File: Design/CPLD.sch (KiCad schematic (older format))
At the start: 1 part, among them U5 5M40ZE64C5N

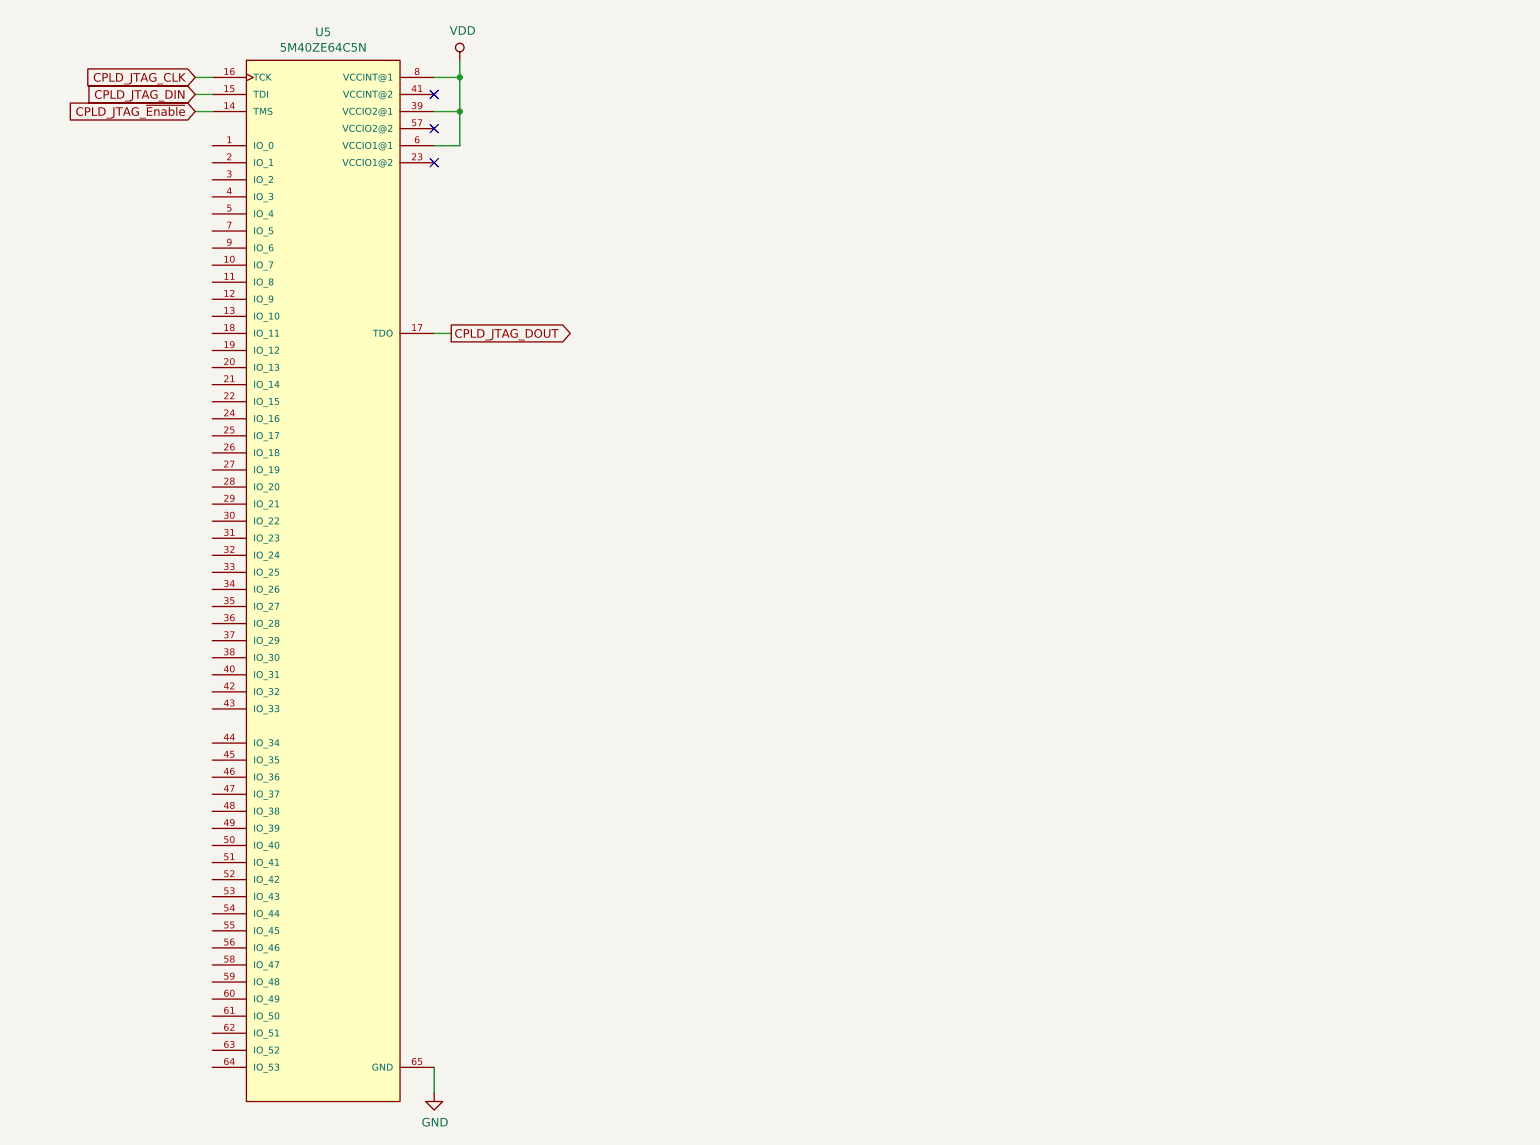
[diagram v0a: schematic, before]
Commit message: Improvement over the Power management: - added TPS6201DRC for raising leaking voltage from supercapacitor - supercap is protected from overvoltage using a shunt diode - power management is using MOSFET logic (2 PFET, 1 NFET)
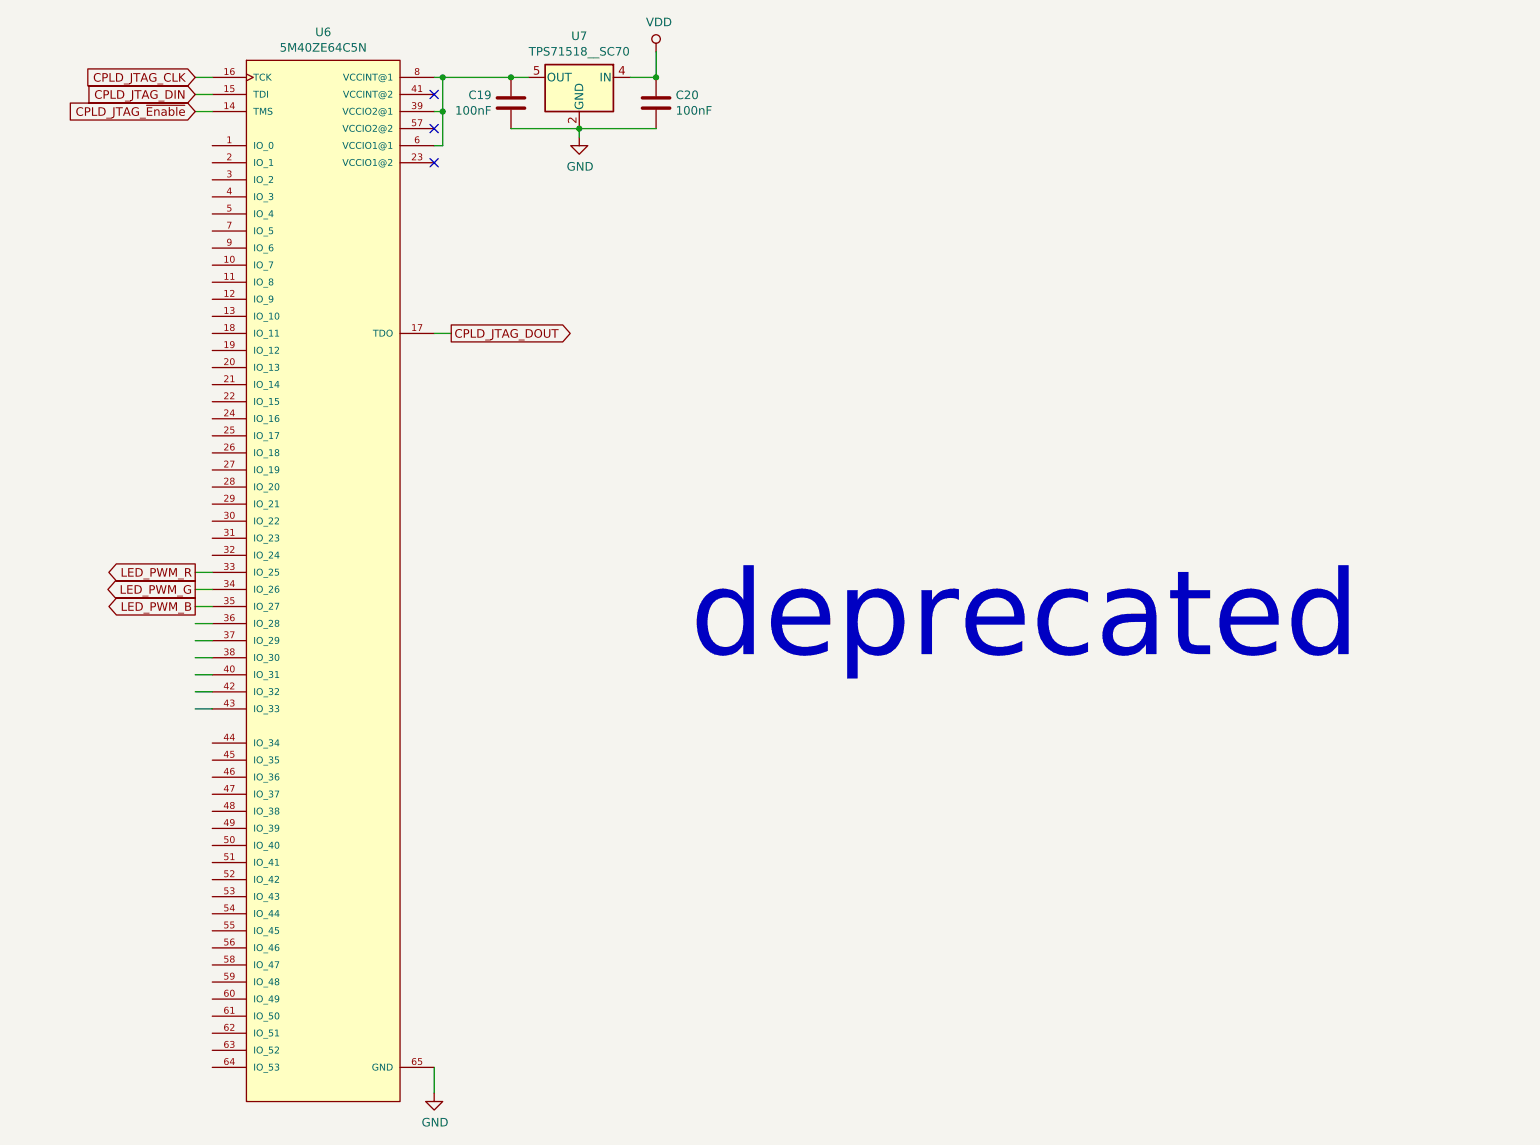
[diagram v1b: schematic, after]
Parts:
- added C19, C20: 100nF, symbol Device:C
- added U7: TPS71518__SC70, Package_TO_SOT_SMD:SOT-353_SC-70-5, symbol Regulator_Linear:TPS71518__SC70
- renumbered U5 to U6
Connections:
- net labels added: LED_PWM_B, LED_PWM_G, LED_PWM_R
- wire segments 11 -> 26
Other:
- note added: "deprecated"
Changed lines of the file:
@@
 $EndDescr
 $Comp
-L Meishi:5M40ZE64C5N U5
+L Meishi:5M40ZE64C5N U6
 U 1 1 5E1FF78D
 P 2300 4000
-F 0 "U5" H 2250 7265 50  0000 C CNN
+F 0 "U6" H 2250 7265 50  0000 C CNN
 F 1 "5M40ZE64C5N" H 2250 7174 50  0000 C CNN
 F 2 "Meishi:QFP40P900X900X120-65N" H 2300 4000 50  0001 L BNN
-F 3 "Altera" H 2300 4000 50  0001 L BNN
+F 3 "https://www.intel.com/content/dam/www/programmable/us/en/pdfs/literature/hb/max-v/mv51003.pdf" H 2300 4000 50  0001 L BNN
 	1    2300 4000
 	1    0    0    -1
 $EndComp
 $Comp
-L power:GND #PWR?
+L power:GND #PWR024
 U 1 1 5E201625
 P 2900 6950
-F 0 "#PWR?" H 2900 6700 50  0001 C CNN
+F 0 "#PWR024" H 2900 6700 50  0001 C CNN
 F 1 "GND" H 2905 6777 50  0000 C CNN
 F 2 "" H 2900 6950 50  0001 C CNN
@@
 	1500 1100 1600 1100
 $Comp
-L power:VDD #PWR?
+L power:VDD #PWR026
 U 1 1 5E2026D0
-P 3050 900
-F 0 "#PWR?" H 3050 750 50  0001 C CNN
-F 1 "VDD" H 3067 1073 50  0000 C CNN
-F 2 "" H 3050 900 50  0001 C CNN
-F 3 "" H 3050 900 50  0001 C CNN
-	1    3050 900
+P 4200 850
+F 0 "#PWR026" H 4200 700 50  0001 C CNN
+F 1 "VDD" H 4217 1023 50  0000 C CNN
+F 2 "" H 4200 850 50  0001 C CNN
+F 3 "" H 4200 850 50  0001 C CNN
+	1    4200 850
 	1    0    0    -1
 $EndComp
 Wire Wire Line
-	3050 900  3050 1000
+	2950 1200 2900 1200
 Wire Wire Line
-	3050 1000 2900 1000
+	2950 1200 2950 1400
 Wire Wire Line
-	3050 1000 3050 1200
-Wire Wire Line
-	3050 1200 2900 1200
-Connection ~ 3050 1000
-Wire Wire Line
-	3050 1200 3050 1400
-Wire Wire Line
-	3050 1400 2900 1400
-Connection ~ 3050 1200
+	2950 1400 2900 1400
 NoConn ~ 2900 1100
 NoConn ~ 2900 1300
 NoConn ~ 2900 1500
+Wire Wire Line
+	1500 4300 1600 4300
+Wire Wire Line
+	1500 4200 1600 4200
+Wire Wire Line
+	1500 4600 1600 4600
+Wire Wire Line
+	1500 4500 1600 4500
+Wire Wire Line
+	1500 4700 1600 4700
+Wire Wire Line
+	1500 4400 1600 4400
+Text GLabel 1500 4000 0    50   Output ~ 0
+LED_PWM_G
+Text GLabel 1500 4100 0    50   Output ~ 0
+LED_PWM_B
+Text GLabel 1500 3900 0    50   Output ~ 0
+LED_PWM_R
+Wire Wire Line
+	1500 3900 1600 3900
+Wire Wire Line
+	1500 4000 1600 4000
+Wire Wire Line
+	1500 4100 1600 4100
+Wire Wire Line
+	4200 850  4200 1000
+$Comp
+L Device:C C20
+U 1 1 5E3E340D
+P 4200 1150
+F 0 "C20" H 4315 1196 50  0000 L CNN
+F 1 "100nF" H 4315 1105 50  0000 L CNN
+F 2 "" H 4238 1000 50  0001 C CNN
+F 3 "~" H 4200 1150 50  0001 C CNN
+	1    4200 1150
+	1    0    0    -1
+$EndComp
+Connection ~ 4200 1000
+$Comp
+L Regulator_Linear:TPS71518__SC70 U7
+U 1 1 5E3E0280
+P 3750 1000
+F 0 "U7" H 3750 1242 50  0000 C CNN
+F 1 "TPS71518__SC70" H 3750 1151 50  0000 C CNN
+F 2 "Package_TO_SOT_SMD:SOT-353_SC-70-5" H 3750 1225 50  0001 C CNN
+F 3 "http://www.ti.com/lit/ds/symlink/tps715.pdf" H 3450 1800 50  0001 C CNN
+	1    3750 1000
+	-1   0    0    -1
+$EndComp
+Wire Wire Line
+	4200 1300 3750 1300
+$Comp
+L power:GND #PWR025
+U 1 1 5E3E28EC
+P 3750 1350
+F 0 "#PWR025" H 3750 1100 50  0001 C CNN
+F 1 "GND" H 3755 1177 50  0000 C CNN
+F 2 "" H 3750 1350 50  0001 C CNN
+F 3 "" H 3750 1350 50  0001 C CNN
+	1    3750 1350
+	1    0    0    -1
+$EndComp
+Wire Wire Line
+	2900 1000 2950 1000
+Connection ~ 3750 1300
+Wire Wire Line
+	3750 1300 3750 1350
+Wire Wire Line
+	4200 1000 4050 1000
+$Comp
+L Device:C C19
+U 1 1 5E3F4EE8
+P 3350 1150
+F 0 "C19" H 3236 1104 50  0000 R CNN
+F 1 "100nF" H 3236 1195 50  0000 R CNN
+F 2 "" H 3388 1000 50  0001 C CNN
+F 3 "~" H 3350 1150 50  0001 C CNN
+	1    3350 1150
+	1    0    0    1
+$EndComp
+Wire Wire Line
+	3450 1000 3350 1000
+Connection ~ 3350 1000
+Wire Wire Line
+	3350 1300 3750 1300
+Wire Wire Line
+	2950 1200 2950 1000
+Connection ~ 2950 1200
+Wire Wire Line
+	2950 1000 3350 1000
+Connection ~ 2950 1000
+Text Notes 4400 4450 0    500  ~ 0
+deprecated
 $EndSCHEMATC
